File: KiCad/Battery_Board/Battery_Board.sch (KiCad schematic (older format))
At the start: 22 parts

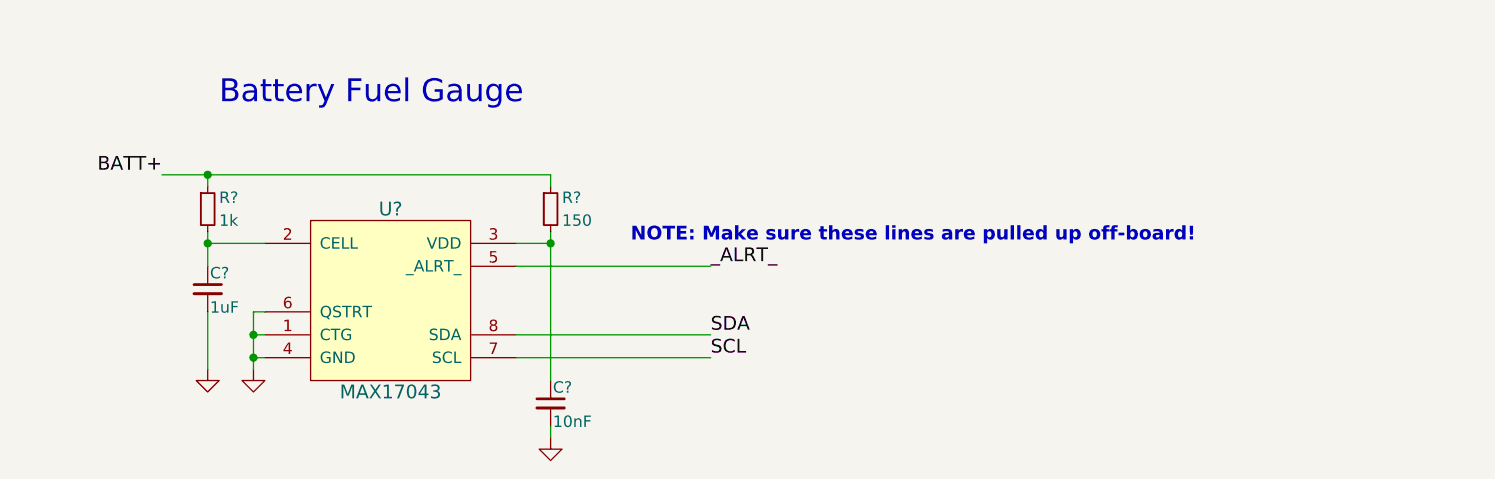
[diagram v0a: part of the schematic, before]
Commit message: Added DNP Pull-Up Resistors.
Just in case there is a need to pull-up the lines on-board.
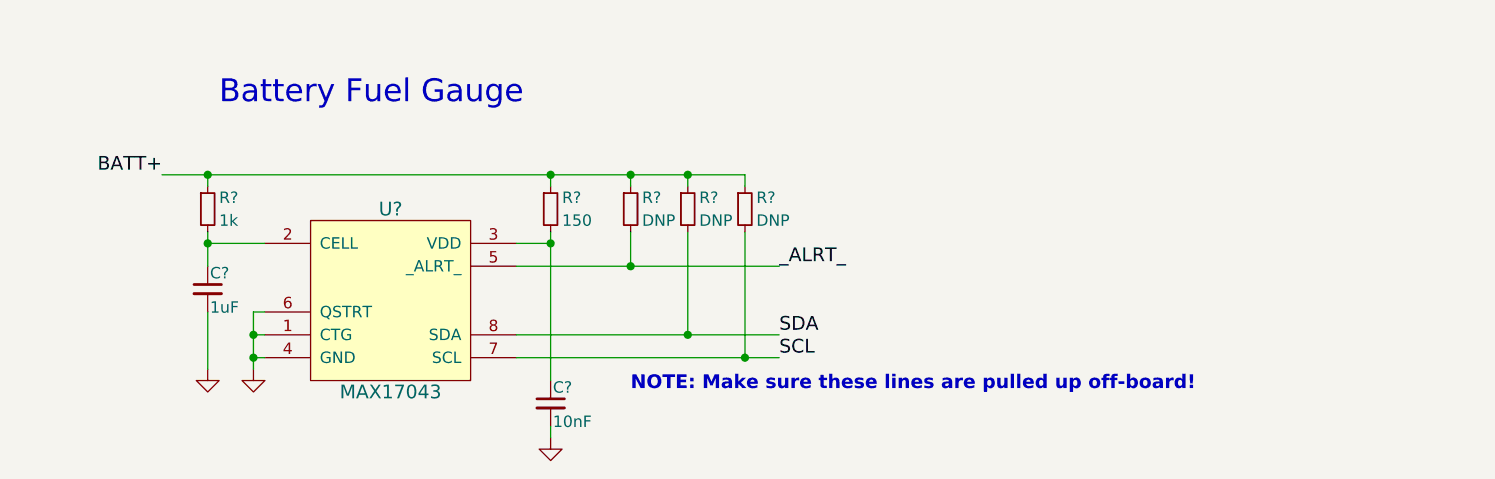
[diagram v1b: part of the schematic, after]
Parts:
- added R? (x3): DNP, symbol R_Small
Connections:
- net BATT+: now also R?.1, R?.1, R?.1
- net SCL: now also R?.2
- net SDA: now also R?.2
- net _ALRT_: now also R?.2
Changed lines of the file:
@@
 	6150 4800 6150 5450
 Wire Wire Line
-	6000 4950 6850 4950
+	6000 4950 7150 4950
 $Comp
 L GND #PWR?
@@
 	6150 5700 6150 5650
 Wire Wire Line
-	6000 5250 6850 5250
+	6000 5250 7150 5250
 Wire Wire Line
-	6000 5350 6850 5350
-Text Label 6850 5250 0    60   ~ 0
+	6000 5350 7150 5350
+Text Label 7150 5250 0    60   ~ 0
 SDA
-Text Label 6850 5350 0    60   ~ 0
+Text Label 7150 5350 0    60   ~ 0
 SCL
 Wire Wire Line
@@
 	4650 4600 4650 4550
 Connection ~ 4650 4550
-Text Label 6850 4950 0    60   ~ 0
+Text Label 7150 4950 0    60   ~ 0
 _ALRT_
 Text Notes 4700 4250 0    100  ~ 0
@@
 	1200 3650 1000 3650
 Wire Wire Line
-	4450 4550 6150 4550
-Text Notes 6500 4850 0    60   ~ 12
+	4450 4550 7000 4550
+Text Notes 6500 5500 0    60   ~ 12
 NOTE: Make sure these lines are pulled up off-board!
+$Comp
+L R_Small R?
+U 1 1 55A29834
+P 6500 4700
+F 0 "R?" H 6550 4750 50  0000 L CNN
+F 1 "DNP" H 6550 4650 50  0000 L CNN
+F 2 "" H 6500 4700 60  0000 C CNN
+F 3 "" H 6500 4700 60  0000 C CNN
+	1    6500 4700
+	1    0    0    -1
+$EndComp
+$Comp
+L R_Small R?
+U 1 1 55A2A0C3
+P 6750 4700
+F 0 "R?" H 6800 4750 50  0000 L CNN
+F 1 "DNP" H 6800 4650 50  0000 L CNN
+F 2 "" H 6750 4700 60  0000 C CNN
+F 3 "" H 6750 4700 60  0000 C CNN
+	1    6750 4700
+	1    0    0    -1
+$EndComp
+$Comp
+L R_Small R?
+U 1 1 55A2A1C5
+P 7000 4700
+F 0 "R?" H 7050 4750 50  0000 L CNN
+F 1 "DNP" H 7050 4650 50  0000 L CNN
+F 2 "" H 7000 4700 60  0000 C CNN
+F 3 "" H 7000 4700 60  0000 C CNN
+	1    7000 4700
+	1    0    0    -1
+$EndComp
+Wire Wire Line
+	6500 4800 6500 4950
+Connection ~ 6500 4950
+Wire Wire Line
+	6750 4800 6750 5250
+Connection ~ 6750 5250
+Wire Wire Line
+	7000 4800 7000 5350
+Connection ~ 7000 5350
+Wire Wire Line
+	7000 4550 7000 4600
+Connection ~ 6150 4550
+Wire Wire Line
+	6750 4600 6750 4550
+Connection ~ 6750 4550
+Wire Wire Line
+	6500 4600 6500 4550
+Connection ~ 6500 4550
 $EndSCHEMATC

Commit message: Created & assigned footprints.
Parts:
- removed D?: LED_RG, symbol LED_RG
- added D1: RG_LED, OpenCamera:RG_LED, symbol RG_LED
- C1, C3, C4: renamed from C?; footprint (none) -> Capacitors_SMD:C_0603
- C2, C5: renamed from C?; footprint (none) -> Capacitors_SMD:C_0805
- P5: renamed from P?; footprint (none) -> OpenCamera:JST-2
- R1, R10, R2, R3, R6, R9: renamed from R?; footprint (none) -> Resistors_SMD:R_0402
- R11, R12, R13, R14, R15, R4, R5, R7, R8: renamed from R?; footprint (none) -> Resistors_SMD:R_0805
- U1: renamed from U?; footprint (none) -> OpenCamera:BQ24230
- U2: renamed from U?; footprint (none) -> OpenCamera:MAX17043
- USB1: renamed from USB?; footprint (none) -> OpenCamera:MicroUSB-B-Receptacle
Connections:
- net Vsys: now also D1.1 (Anode); no longer R10.2, R9.2
- net at U1.7 (_PGOOD_): now also R9.1
- net at U1.9 (_CHG_): now also R10.1
- new net: D1.2 (RED_CATHODE), R10.2
- new net: D1.3 (GREEN_CATHODE), R9.2
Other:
- moved on the sheet: R10, R9

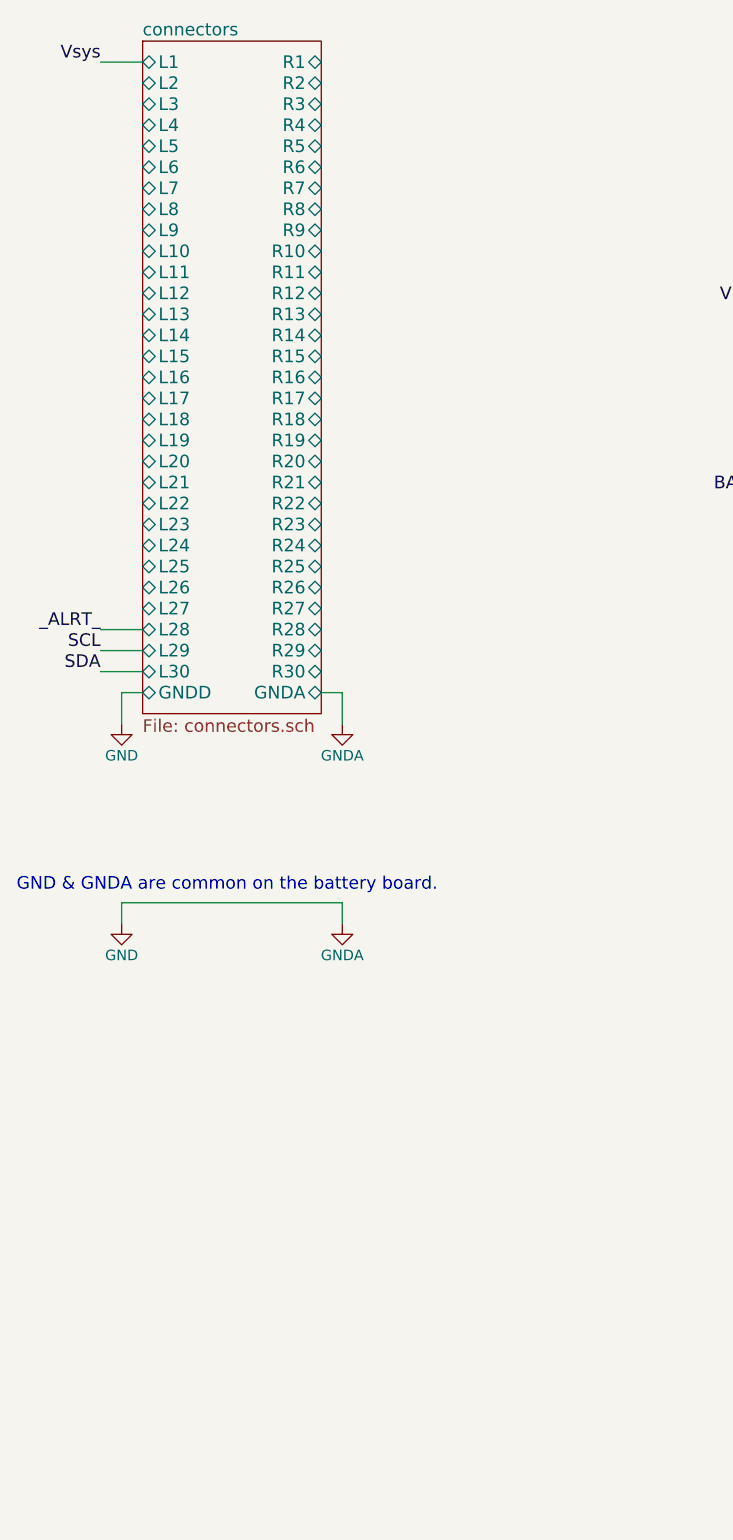
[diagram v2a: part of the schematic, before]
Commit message: Added power switch.
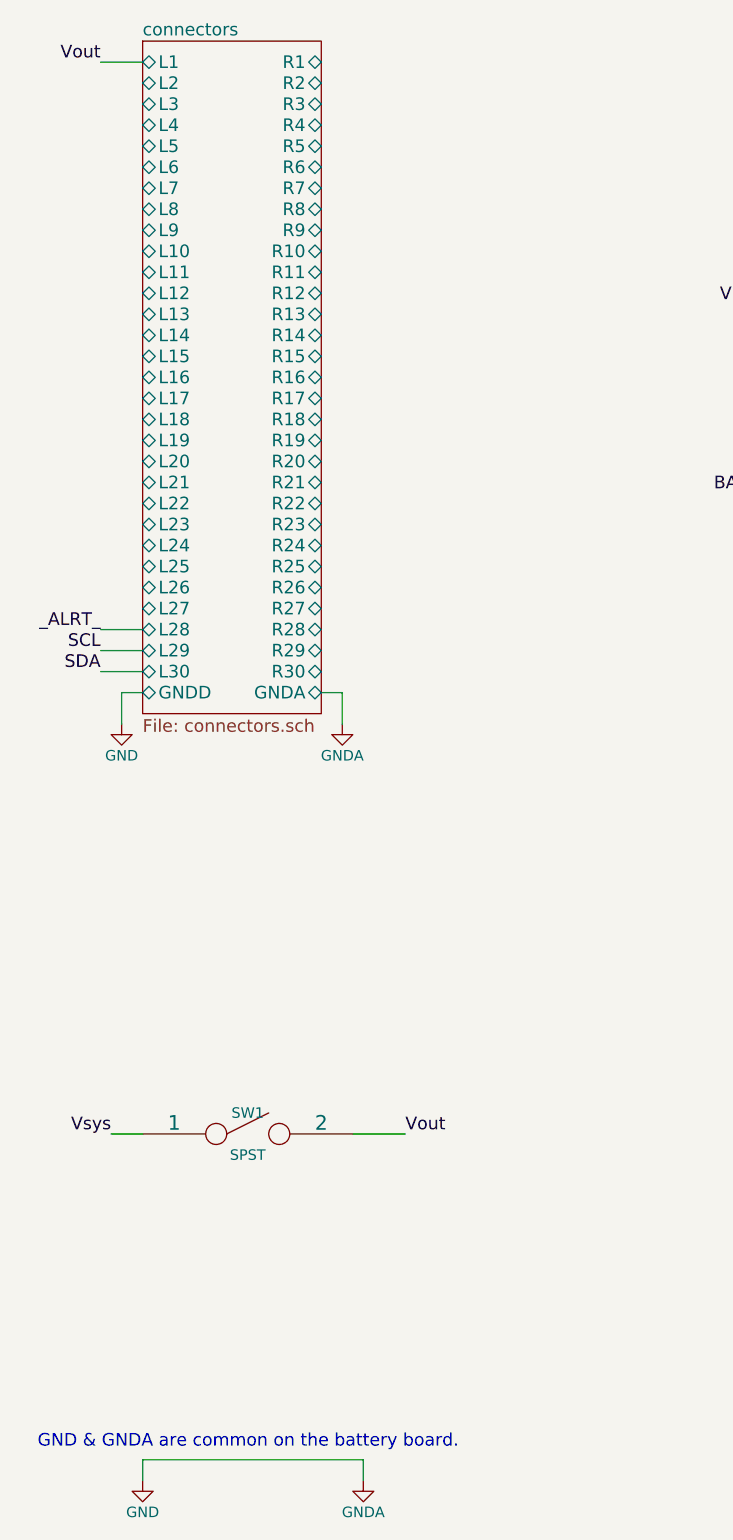
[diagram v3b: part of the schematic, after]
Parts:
- added SW1: SPST, OpenCamera:SWITCH_SPST, symbol SPST
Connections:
- net Vsys: now also SW1.1
- new net Vout: SW1.2
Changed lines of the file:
@@
 L GNDA #PWR03
 U 1 1 55A2ED6E
-P 2150 4850
-F 0 "#PWR03" H 2150 4600 50  0001 C CNN
-F 1 "GNDA" H 2150 4700 50  0000 C CNN
-F 2 "" H 2150 4850 60  0000 C CNN
-F 3 "" H 2150 4850 60  0000 C CNN
-	1    2150 4850
+P 2250 7500
+F 0 "#PWR03" H 2250 7250 50  0001 C CNN
+F 1 "GNDA" H 2250 7350 50  0000 C CNN
+F 2 "" H 2250 7500 60  0000 C CNN
+F 3 "" H 2250 7500 60  0000 C CNN
+	1    2250 7500
 	1    0    0    -1
 $EndComp
@@
 L GND #PWR04
 U 1 1 55A2F061
-P 1100 4850
-F 0 "#PWR04" H 1100 4600 50  0001 C CNN
-F 1 "GND" H 1100 4700 50  0000 C CNN
-F 2 "" H 1100 4850 60  0000 C CNN
-F 3 "" H 1100 4850 60  0000 C CNN
-	1    1100 4850
-	1    0    0    -1
-$EndComp
-Wire Wire Line
-	1100 4850 1100 4750
-Wire Wire Line
-	1100 4750 2150 4750
-Wire Wire Line
-	2150 4750 2150 4850
-Text Notes 600  4700 0    60   ~ 0
+P 1200 7500
+F 0 "#PWR04" H 1200 7250 50  0001 C CNN
+F 1 "GND" H 1200 7350 50  0000 C CNN
+F 2 "" H 1200 7500 60  0000 C CNN
+F 3 "" H 1200 7500 60  0000 C CNN
+	1    1200 7500
+	1    0    0    -1
+$EndComp
+Wire Wire Line
+	1200 7500 1200 7400
+Wire Wire Line
+	1200 7400 2250 7400
+Wire Wire Line
+	2250 7400 2250 7500
+Text Notes 700  7350 0    60   ~ 0
 GND & GNDA are common on the battery board.
 $Comp
@@
 	4900 5250 4850 5250
 Connection ~ 4850 5250
-Text Label 1000 750  2    60   ~ 0
+Text Label 1050 5850 2    60   ~ 0
 Vsys
 Text Label 4450 4550 2    60   ~ 0
@@
 Wire Wire Line
 	6950 1250 6950 1900
+$Comp
+L SPST SW1
+U 1 1 55A327CA
+P 1700 5850
+F 0 "SW1" H 1700 5950 50  0000 C CNN
+F 1 "SPST" H 1700 5750 50  0000 C CNN
+F 2 "OpenCamera:SWITCH_SPST" H 1700 5850 60  0001 C CNN
+F 3 "" H 1700 5850 60  0000 C CNN
+	1    1700 5850
+	1    0    0    -1
+$EndComp
+Wire Wire Line
+	1050 5850 1200 5850
+Text Label 2450 5850 0    60   ~ 0
+Vout
+Wire Wire Line
+	2200 5850 2450 5850
+Text Label 1000 750  2    60   ~ 0
+Vout
 $EndSCHEMATC

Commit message: Initial part placement.
Also added cutouts around the battery for a battery strap.
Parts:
- R12, R14, R4, R5, R8: footprint Resistors_SMD:R_0805 -> Resistors_SMD:R_0402
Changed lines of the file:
@@
 F 0 "R5" H 5700 3450 50  0000 L CNN
 F 1 "DNP" H 5700 3350 50  0000 L CNN
-F 2 "Resistors_SMD:R_0805" H 5650 3400 60  0001 C CNN
+F 2 "Resistors_SMD:R_0402" H 5650 3400 60  0001 C CNN
 F 3 "" H 5650 3400 60  0000 C CNN
 	1    5650 3400
@@
 F 0 "R4" H 5450 3450 50  0000 L CNN
 F 1 "DNP" H 5450 3350 50  0000 L CNN
-F 2 "Resistors_SMD:R_0805" H 5400 3400 60  0001 C CNN
+F 2 "Resistors_SMD:R_0402" H 5400 3400 60  0001 C CNN
 F 3 "" H 5400 3400 60  0000 C CNN
 	1    5400 3400
@@
 F 0 "R8" H 6550 4750 50  0000 L CNN
 F 1 "DNP" H 6550 4650 50  0000 L CNN
-F 2 "Resistors_SMD:R_0805" H 6500 4700 60  0001 C CNN
+F 2 "Resistors_SMD:R_0402" H 6500 4700 60  0001 C CNN
 F 3 "" H 6500 4700 60  0000 C CNN
 	1    6500 4700
@@
 F 0 "R12" H 6800 4750 50  0000 L CNN
 F 1 "DNP" H 6800 4650 50  0000 L CNN
-F 2 "Resistors_SMD:R_0805" H 6750 4700 60  0001 C CNN
+F 2 "Resistors_SMD:R_0402" H 6750 4700 60  0001 C CNN
 F 3 "" H 6750 4700 60  0000 C CNN
 	1    6750 4700
@@
 F 0 "R14" H 7050 4750 50  0000 L CNN
 F 1 "DNP" H 7050 4650 50  0000 L CNN
-F 2 "Resistors_SMD:R_0805" H 7000 4700 60  0001 C CNN
+F 2 "Resistors_SMD:R_0402" H 7000 4700 60  0001 C CNN
 F 3 "" H 7000 4700 60  0000 C CNN
 	1    7000 4700
